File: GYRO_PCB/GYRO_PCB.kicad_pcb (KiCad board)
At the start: 2 copper layers, 72.4 x 57.2 mm, 18 parts, among them J1 Pmod GYRO, J2 FLASH Socket 1, J3 FLASH Socket 2, J4 Power Terminal, U1 NUCLEO64-F446RE

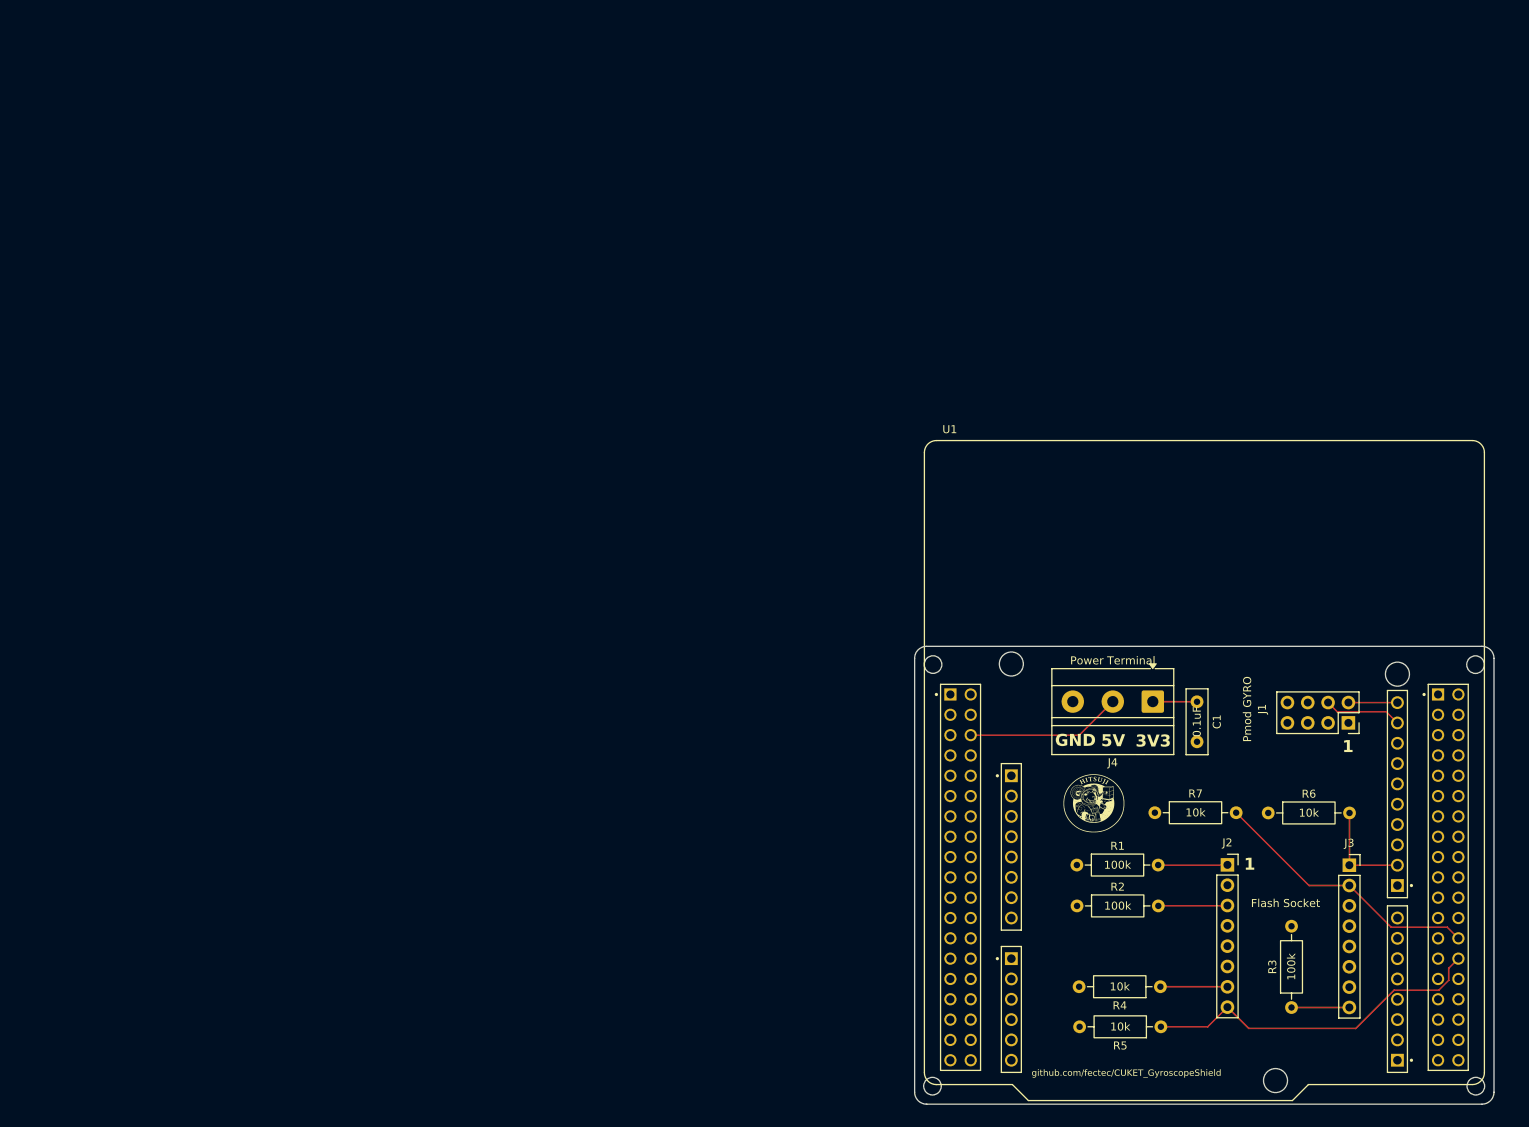
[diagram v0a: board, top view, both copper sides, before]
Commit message: New schematic
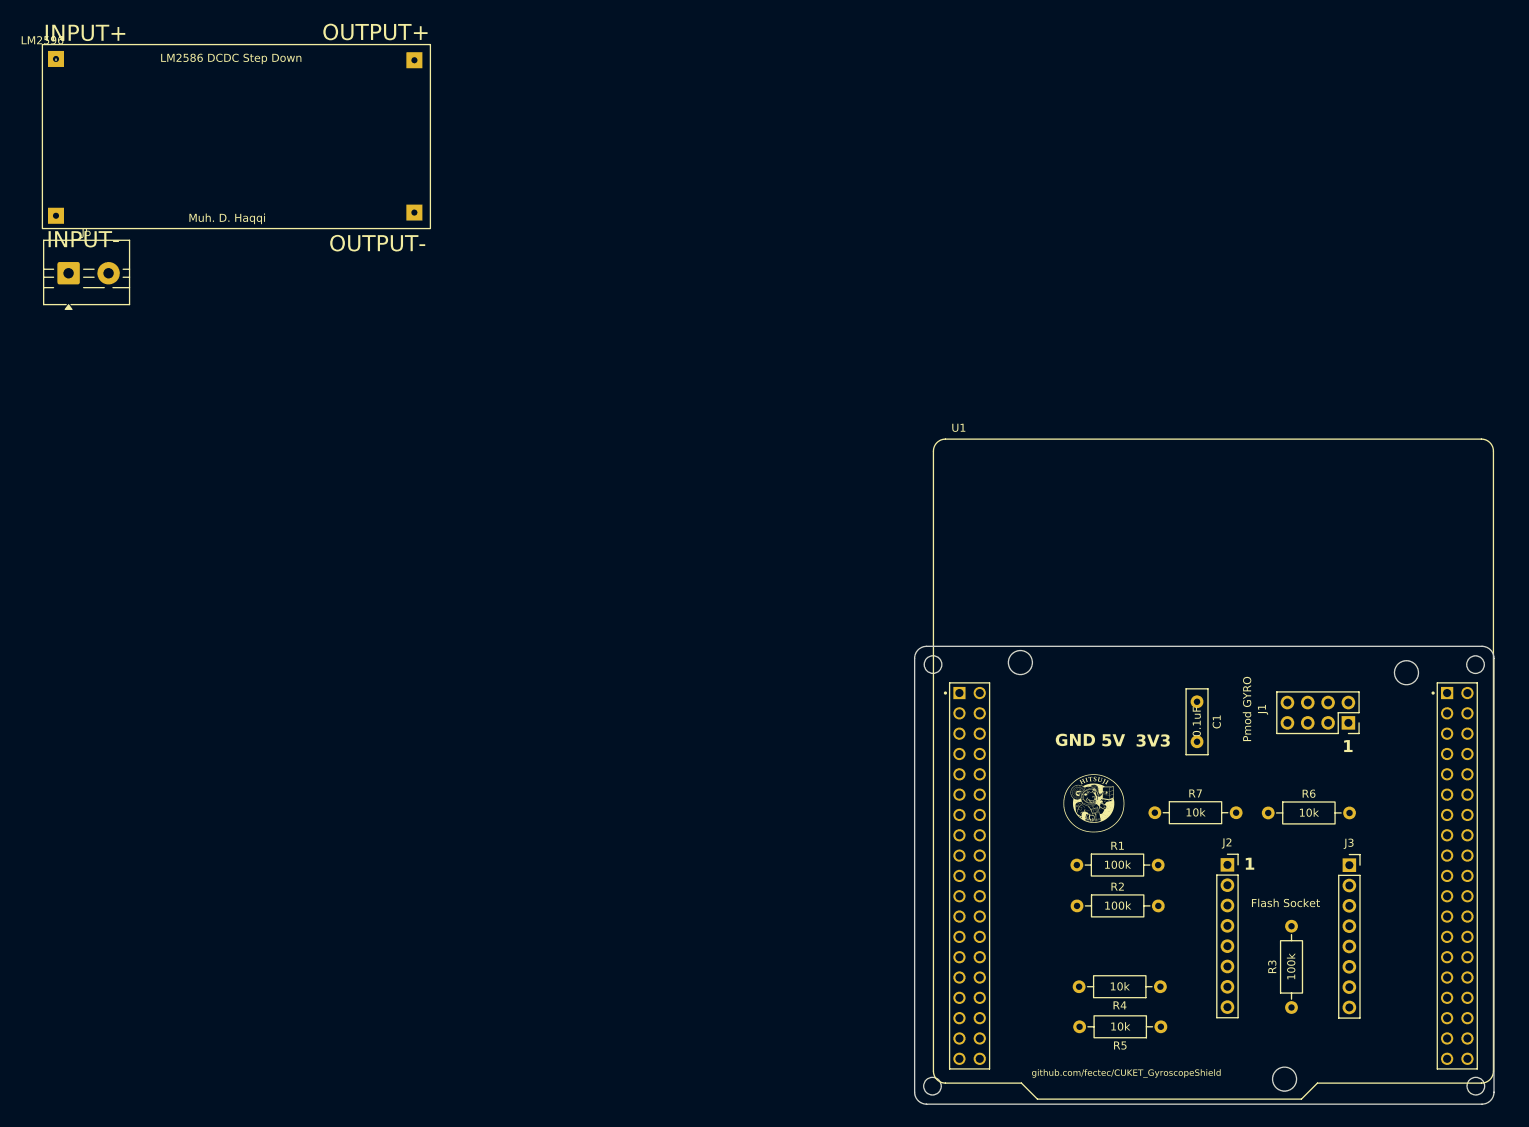
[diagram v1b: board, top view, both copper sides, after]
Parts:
- removed J4: Power Terminal, TerminalBlock_MetzConnect:TerminalBlock_MetzConnect_Type011_RT05503HBLC_1x03_P5.00mm_Horizontal
- added J5: Power Terminal - Raw, TerminalBlock:TerminalBlock_MaiXu_MX126-5.0-02P_1x02_P5.00mm, F.Cu at (3.52, 28.8)
- added LM2596: ~, FOOTPRINTS:LM2596 Module, F.Cu at (0.25, 0.25)
- moved U1 1.14 mm to (146.6, 90.8)
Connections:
- U1 pad CN10_1: (no net) -> unconnected-(U1-PC9-PadCN10_1)
- U1 pad CN10_10: (no net) -> unconnected-(U1-NC-PadCN10_10)
- U1 pad CN10_11: (no net) -> unconnected-(U1-PA5-PadCN10_11)
- U1 pad CN10_12: (no net) -> unconnected-(U1-PA12-PadCN10_12)
- U1 pad CN10_13: (no net) -> unconnected-(U1-PA6-PadCN10_13)
- U1 pad CN10_14: (no net) -> unconnected-(U1-PA11-PadCN10_14)
- U1 pad CN10_15: (no net) -> unconnected-(U1-PA7-PadCN10_15)
- U1 pad CN10_16: (no net) -> unconnected-(U1-PB12-PadCN10_16)
- U1 pad CN10_17: (no net) -> unconnected-(U1-PB6-PadCN10_17)
- U1 pad CN10_18: (no net) -> unconnected-(U1-NC-PadCN10_18)
- U1 pad CN10_19: (no net) -> NUCLEO_FLASH_SCLK
- U1 pad CN10_2: (no net) -> unconnected-(U1-PC8-PadCN10_2)
- U1 pad CN10_20: (no net) -> unconnected-(U1-GND-PadCN10_20)
- U1 pad CN10_21: (no net) -> unconnected-(U1-PA9-PadCN10_21)
- U1 pad CN10_22: (no net) -> unconnected-(U1-PB2-PadCN10_22)
- U1 pad CN10_23: (no net) -> unconnected-(U1-PA8-PadCN10_23)
- U1 pad CN10_24: (no net) -> unconnected-(U1-PB1-PadCN10_24)
- U1 pad CN10_25: (no net) -> unconnected-(U1-PB10-PadCN10_25)
- U1 pad CN10_27: (no net) -> unconnected-(U1-PB4-PadCN10_27)
- U1 pad CN10_29: (no net) -> unconnected-(U1-PB5-PadCN10_29)
- U1 pad CN10_3: (no net) -> NUCLEO_GYRO_I2C1_SCL
- U1 pad CN10_30: (no net) -> unconnected-(U1-PB13-PadCN10_30)
- U1 pad CN10_31: (no net) -> unconnected-(U1-STLINK_SWO/PB3-PadCN10_31)
- U1 pad CN10_32: (no net) -> unconnected-(U1-AGND-PadCN10_32)
- U1 pad CN10_33: (no net) -> unconnected-(U1-PA10-PadCN10_33)
- U1 pad CN10_34: (no net) -> unconnected-(U1-PC4-PadCN10_34)
- U1 pad CN10_35: (no net) -> unconnected-(U1-STLINK_UART_TX/PA2-PadCN10_35)
- U1 pad CN10_36: (no net) -> unconnected-(U1-NC-PadCN10_36)
- U1 pad CN10_37: (no net) -> unconnected-(U1-STLINK_UART_RX/PA3-PadCN10_37)
- U1 pad CN10_38: (no net) -> unconnected-(U1-NC-PadCN10_38)
- U1 pad CN10_4: (no net) -> unconnected-(U1-PC6-PadCN10_4)
- U1 pad CN10_5: (no net) -> NUCLEO_GYRO_I2C1_SDA
- U1 pad CN10_6: (no net) -> unconnected-(U1-PC5-PadCN10_6)
- U1 pad CN10_7: (no net) -> unconnected-(U1-AVDD-PadCN10_7)
- U1 pad CN10_8: (no net) -> unconnected-(U1-U5V-PadCN10_8)
- U1 pad CN10_9: (no net) -> unconnected-(U1-GND-PadCN10_9)
- U1 pad CN7_1: (no net) -> unconnected-(U1-PC10-PadCN7_1)
- U1 pad CN7_10: (no net) -> unconnected-(U1-NC-PadCN7_10)
- U1 pad CN7_11: (no net) -> unconnected-(U1-NC-PadCN7_11)
- U1 pad CN7_12: (no net) -> NUCLEO_E5V
- U1 pad CN7_13: (no net) -> unconnected-(U1-STLINK_TMS/PA13-PadCN7_13)
- U1 pad CN7_14: (no net) -> unconnected-(U1-~{RESET}-PadCN7_14)
- U1 pad CN7_15: (no net) -> unconnected-(U1-STLINK_TCK/PA14-PadCN7_15)
- U1 pad CN7_16: (no net) -> unconnected-(U1-+3V3-PadCN7_16)
- U1 pad CN7_17: (no net) -> unconnected-(U1-PA15-PadCN7_17)
- U1 pad CN7_18: (no net) -> +3V3
- U1 pad CN7_19: (no net) -> unconnected-(U1-GND-PadCN7_19)
- U1 pad CN7_2: (no net) -> unconnected-(U1-PC11-PadCN7_2)
- U1 pad CN7_20: (no net) -> unconnected-(U1-GND-PadCN7_20)
- U1 pad CN7_21: (no net) -> unconnected-(U1-PB7-PadCN7_21)
- U1 pad CN7_22: (no net) -> unconnected-(U1-GND-PadCN7_22)
- U1 pad CN7_23: (no net) -> unconnected-(U1-PC13-PadCN7_23)
- U1 pad CN7_24: (no net) -> unconnected-(U1-VIN-PadCN7_24)
- U1 pad CN7_25: (no net) -> unconnected-(U1-PC14-PadCN7_25)
- U1 pad CN7_26: (no net) -> unconnected-(U1-NC-PadCN7_26)
- U1 pad CN7_27: (no net) -> unconnected-(U1-PC15-PadCN7_27)
- U1 pad CN7_28: (no net) -> unconnected-(U1-PA0-PadCN7_28)
- U1 pad CN7_29: (no net) -> unconnected-(U1-PH0-PadCN7_29)
- U1 pad CN7_3: (no net) -> unconnected-(U1-PC12-PadCN7_3)
- U1 pad CN7_30: (no net) -> unconnected-(U1-PA1-PadCN7_30)
- U1 pad CN7_31: (no net) -> unconnected-(U1-PH1-PadCN7_31)
- U1 pad CN7_32: (no net) -> NUCLEO_FLASH_CS
- U1 pad CN7_33: (no net) -> unconnected-(U1-VBAT-PadCN7_33)
- U1 pad CN7_34: (no net) -> unconnected-(U1-PB0-PadCN7_34)
- U1 pad CN7_35: (no net) -> unconnected-(U1-PC2-PadCN7_35)
- U1 pad CN7_36: (no net) -> unconnected-(U1-PC1-PadCN7_36)
- U1 pad CN7_37: (no net) -> unconnected-(U1-PC3-PadCN7_37)
- U1 pad CN7_38: (no net) -> unconnected-(U1-PC0-PadCN7_38)
- U1 pad CN7_4: (no net) -> unconnected-(U1-PD2-PadCN7_4)
- U1 pad CN7_5: (no net) -> unconnected-(U1-VDD-PadCN7_5)
- U1 pad CN7_6: NUCLEO_E5V -> unconnected-(U1-E5V-PadCN7_6)
- U1 pad CN7_7: (no net) -> unconnected-(U1-~{BOOT0}-PadCN7_7)
- U1 pad CN7_8: (no net) -> unconnected-(U1-GND-PadCN7_8)
- U1 pad CN7_9: (no net) -> unconnected-(U1-NC-PadCN7_9)
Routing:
- net NUCLEO_FLASH_SPI2_MISO: track 43.8 -> 0.00 mm
- net NUCLEO_FLASH_SPI2_MOSI: track 34.3 -> 0.00 mm
- net NUCLEO_E5V: track 19.5 -> 0.00 mm
- net NUCLEO_FLASH_SCLK: track 12.5 -> 0.00 mm
- net NUCLEO_GYRO_I2C1_SDA: track 9.73 -> 0.00 mm
- net Net-(J2-DQ3/HOLD#): track 8.67 -> 0.00 mm
- net Net-(J2-RESET#): track 8.66 -> 0.00 mm
- net NUCLEO_FLASH_CS: track 8.38 -> 0.00 mm
- net Net-(J3-W#/DQ2): track 7.23 -> 0.00 mm
- net NUCLEO_GYRO_I2C1_SCL: track 6.13 -> 0.00 mm

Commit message: new pcb and schematic
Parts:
- removed H1, H2, H3, H4: MountingHole, MountingHole:MountingHole_2.2mm_M2_ISO14580
- added D1: SFH4346, LED_THT:LED_D3.0mm_IRBlack, F.Cu at (127.0, 86.3)
- added J4: Switch Bat, TerminalBlock:TerminalBlock_MaiXu_MX126-5.0-02P_1x02_P5.00mm, F.Cu at (120.0, 75.0)
- added R8: 330, Resistor_THT:R_Axial_DIN0207_L6.3mm_D2.5mm_P10.16mm_Horizontal, F.Cu at (136.5, 89.6)
- moved LM2596 140.2 mm to (130.3, 52.6)
- moved J5 120.6 mm to (120.0, 60.0), turned to 90 degrees
- moved R3 18.3 mm to (139.7, 113.0), turned to 180 degrees
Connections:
- J5 pad 1: BAT -> Net-(J4-Pin_2)
- U1 pad CN7_12: NUCLEO_E5V -> unconnected-(U1-IOREF-PadCN7_12)
- U1 pad CN7_16: unconnected-(U1-+3V3-PadCN7_16) -> +3V3
- U1 pad CN7_17: unconnected-(U1-PA15-PadCN7_17) -> LED
- U1 pad CN7_18: +3V3 -> unconnected-(U1-+5V-PadCN7_18)
- U1 pad CN7_6: unconnected-(U1-E5V-PadCN7_6) -> NUCLEO_E5V
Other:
- board size 72.4 x 57.2 mm -> 74.5 x 84 mm
- board text removed: "3V3"
- board text removed: "5V"
- board text removed: "GND"

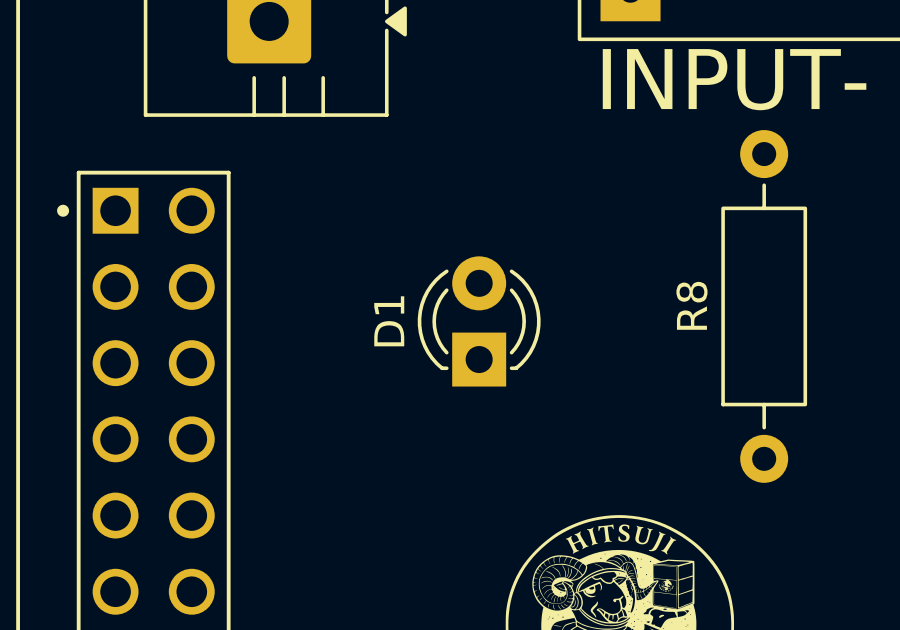
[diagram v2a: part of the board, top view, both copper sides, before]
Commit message: updated footprint for LED
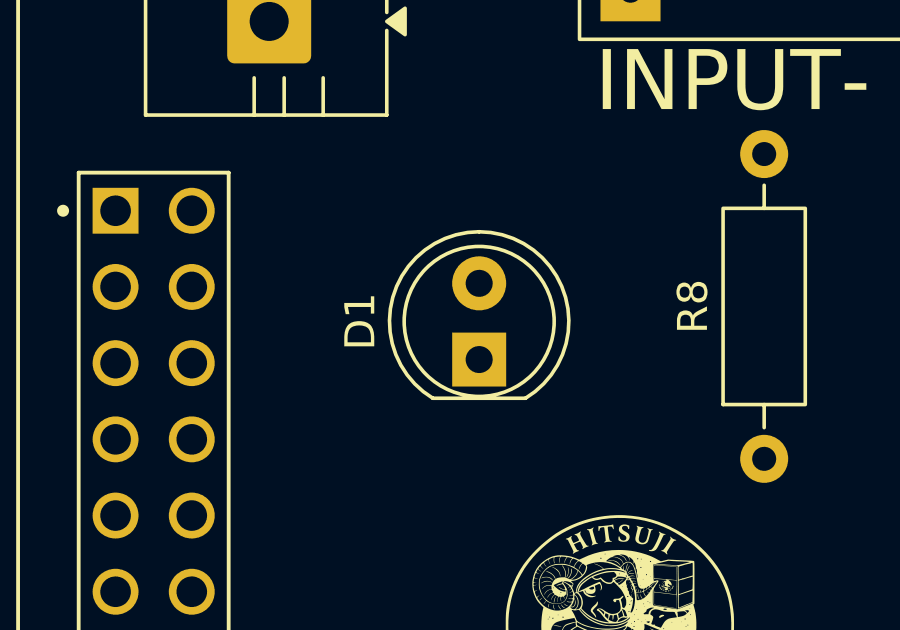
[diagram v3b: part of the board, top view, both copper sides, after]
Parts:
- D1: footprint LED_THT:LED_D3.0mm_IRBlack -> LED_THT:LED_D5.0mm_IRBlack
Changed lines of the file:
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@@
 		)
 	)
-	(footprint "LED_THT:LED_D3.0mm_IRBlack"
+	(footprint "LED_THT:LED_D5.0mm_IRBlack"
 		(layer "F.Cu")
 		(at 127 86.27 90)
-		(descr "LED, diameter 3.0mm, 2 pins, infrared, black, generated by kicad-footprint-generator")
+		(descr "LED, diameter 5.0mm, 2 pins, infrared, black, http://cdn-reichelt.de/documents/datenblatt/A500/LL-504BC2E-009.pdf, generated by kicad-footprint-generator")
 		(tags "LED IR")
 		(property "Reference" "D1"
-			(at 1.27 -2.96 90)
+			(at 1.27 -3.96 90)
 			(layer "F.SilkS")
 			(effects
@@
 		)
 		(property "Value" "SFH4346"
-			(at 1.27 2.96 90)
+			(at 1.27 3.96 90)
 			(layer "F.Fab")
 			(effects
@@
 		(attr through_hole)
 		(fp_line
-			(start -0.29 -1.236)
-			(end -0.29 -1.08)
-			(stroke
-				(width 0.12)
-				(type solid)
-			)
-			(layer "F.SilkS")
-		)
-		(fp_line
-			(start -0.29 1.08)
-			(end -0.29 1.236)
+			(start -1.29 -1.545)
+			(end -1.29 1.545)
 			(stroke
 				(width 0.12)
@@
 		)
 		(fp_arc
-			(start -0.29 -1.235516)
-			(mid 1.36566 -1.987699)
-			(end 2.941437 -1.08)
+			(start -1.29 -1.54483)
+			(mid 2.071779 -2.880495)
+			(end 4.26 0)
 			(stroke
 				(width 0.12)
@@
 		)
 		(fp_arc
-			(start 0.229039 -1.08)
-			(mid 1.27 -1.5)
-			(end 2.310961 -1.08)
+			(start 4.26 0)
+			(mid 2.071779 2.880495)
+			(end -1.29 1.54483)
 			(stroke
 				(width 0.12)
@@
 			(layer "F.SilkS")
 		)
-		(fp_arc
-			(start 2.941437 1.08)
-			(mid 1.36566 1.987699)
-			(end -0.29 1.235516)
+		(fp_circle
+			(center 1.27 0)
+			(end 3.77 0)
 			(stroke
 				(width 0.12)
 				(type solid)
 			)
-			(layer "F.SilkS")
-		)
-		(fp_arc
-			(start 2.310961 1.08)
-			(mid 1.27 1.5)
-			(end 0.229039 1.08)
-			(stroke
-				(width 0.12)
-				(type solid)
-			)
+			(fill no)
 			(layer "F.SilkS")
 		)
 		(fp_line
-			(start 3.69 -2.21)
-			(end -1.15 -2.21)
+			(start 4.49 -3.21)
+			(end -1.94 -3.21)
 			(stroke
 				(width 0.05)
@@
 		)
 		(fp_line
-			(start -1.15 -2.21)
-			(end -1.15 2.21)
+			(start -1.94 -3.21)
+			(end -1.94 3.21)
 			(stroke
 				(width 0.05)
@@
 		)
 		(fp_line
-			(start 3.69 2.21)
-			(end 3.69 -2.21)
+			(start 4.49 3.21)
+			(end 4.49 -3.21)
 			(stroke
 				(width 0.05)
@@
 		)
 		(fp_line
-			(start -1.15 2.21)
-			(end 3.69 2.21)
+			(start -1.94 3.21)
+			(end 4.49 3.21)
 			(stroke
 				(width 0.05)
@@
 		)
 		(fp_line
-			(start -0.23 -1.16619)
-			(end -0.23 1.16619)
+			(start -1.23 -1.469694)
+			(end -1.23 1.469694)
 			(stroke
 				(width 0.1)
@@
 		)
 		(fp_arc
-			(start -0.23 -1.16619)
-			(mid 3.17 0)
-			(end -0.23 1.16619)
+			(start -1.23 -1.469694)
+			(mid 4.17 0)
+			(end -1.23 1.469694)
 			(stroke
 				(width 0.1)
@@
 		(fp_circle
 			(center 1.27 0)
-			(end 2.77 0)
+			(end 3.77 0)
 			(stroke
 				(width 0.1)
@@
 		)
 		(embedded_fonts no)
-		(model "${KICAD9_3DMODEL_DIR}/LED_THT.3dshapes/LED_D3.0mm_IRBlack.step"
+		(model "${KICAD9_3DMODEL_DIR}/LED_THT.3dshapes/LED_D5.0mm_IRBlack.step"
 			(offset
 				(xyz 0 0 0)
